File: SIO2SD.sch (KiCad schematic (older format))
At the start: 17 parts, among them J203 Micro_SD_Card, J204 ISP, J205 SIO, J206 SIOLED, U200 ATmega32-16AU, U201 74HC245, U202 LM2936-3.3, Y200 Crystal

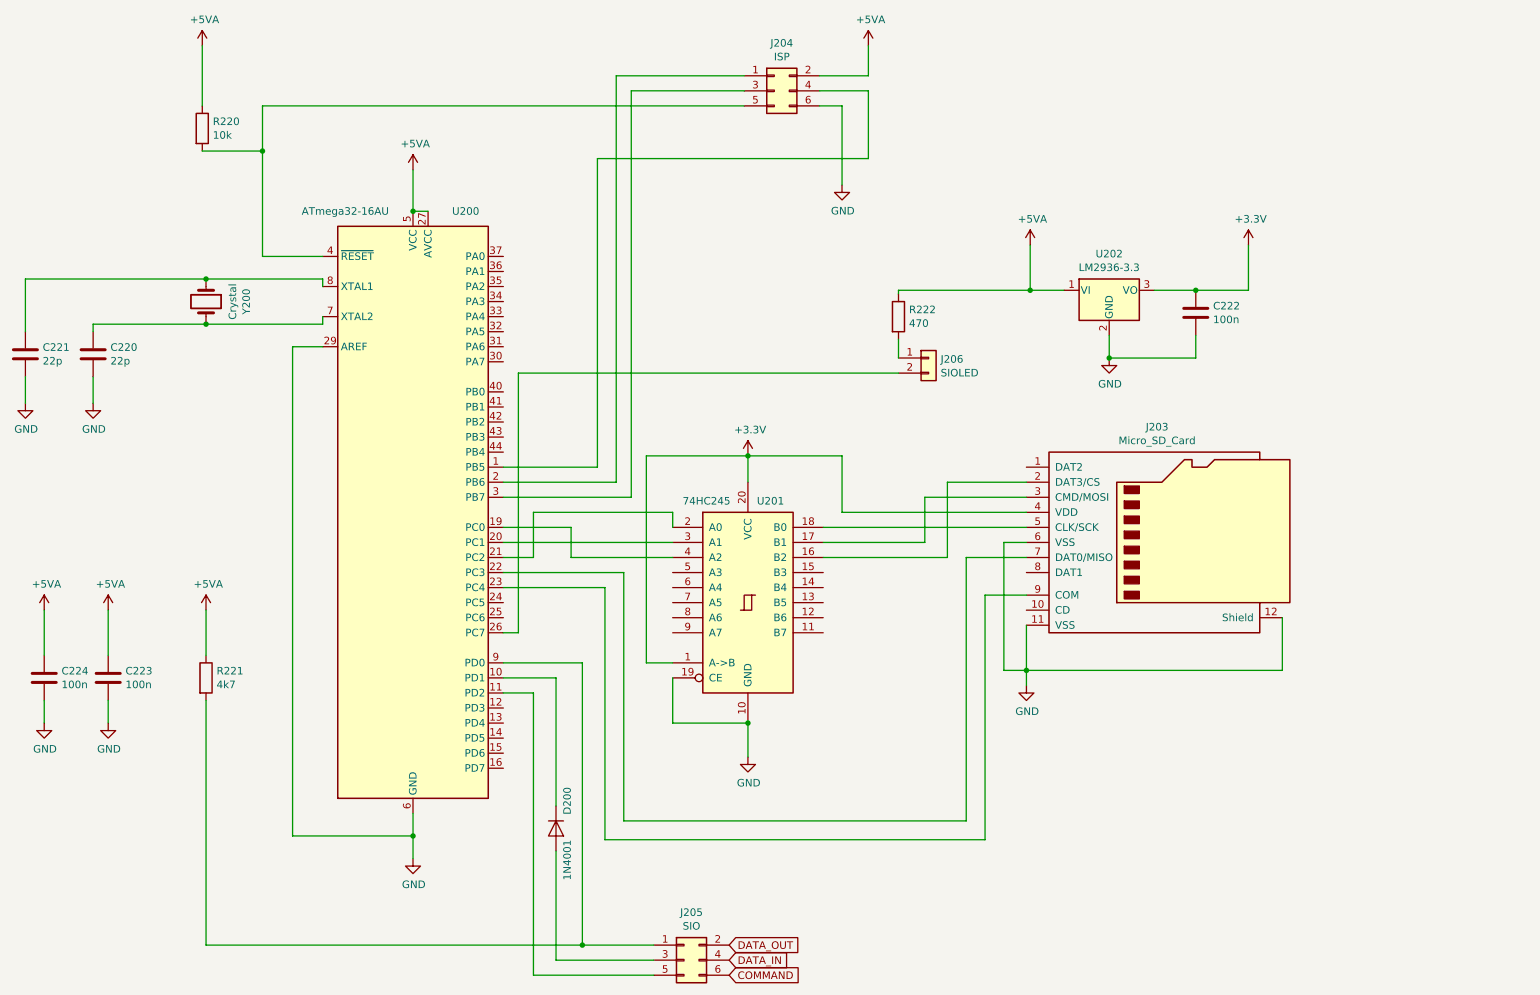
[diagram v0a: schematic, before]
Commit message: Final Atmega32
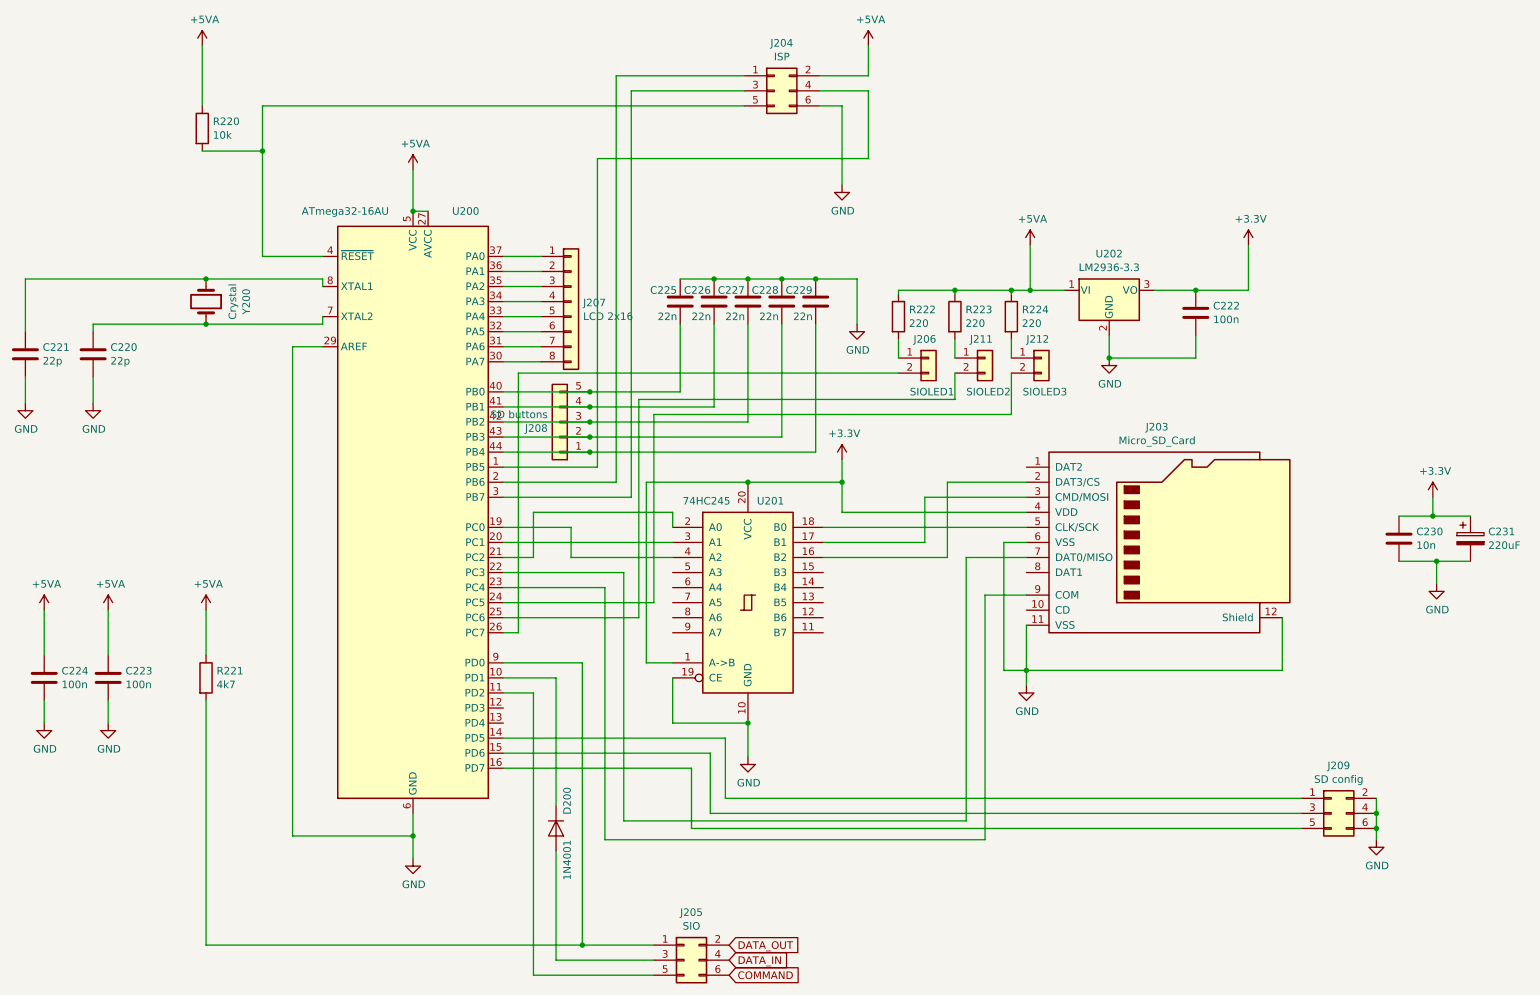
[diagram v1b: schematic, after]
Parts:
- added C225, C226, C227, C228, C229: 22n, Capacitor_SMD:C_1206_3216Metric_Pad1.42x1.75mm_HandSolder, symbol Device:C
- added C230: 10n, Capacitor_SMD:C_1206_3216Metric_Pad1.42x1.75mm_HandSolder, symbol Device:C
- added C231: 220uF, Capacitor_Tantalum_SMD:CP_EIA-7343-40_Kemet-Y_Pad2.25x2.55mm_HandSolder, symbol Device:CP
- added J207: LCD 2x16, Connector_PinHeader_2.54mm:PinHeader_1x08_P2.54mm_Vertical, symbol Connector_Generic:Conn_01x08
- added J208: SD buttons, Connector_PinHeader_2.54mm:PinHeader_1x05_P2.54mm_Vertical, symbol Connector_Generic:Conn_01x05
- added J209: SD config, Connector_PinHeader_2.54mm:PinHeader_2x03_P2.54mm_Vertical, symbol Connector_Generic:Conn_02x03_Odd_Even
- added J211: SIOLED2, Connector_PinHeader_2.54mm:PinHeader_1x02_P2.54mm_Vertical, symbol Connector_Generic:Conn_01x02
- added J212: SIOLED3, Connector_PinHeader_2.54mm:PinHeader_1x02_P2.54mm_Vertical, symbol Connector_Generic:Conn_01x02
- added R223, R224: 220, Resistor_SMD:R_1206_3216Metric_Pad1.42x1.75mm_HandSolder, symbol Device:R
- J206: value SIOLED -> SIOLED1
- R222: value 470 -> 220
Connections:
- net +3V3: now also C230.1, C231.1
- net +5VA: now also R223.1, R224.1
- net GND: now also C225.1, C226.1, C227.1, C228.1, C229.1, C230.2, C231.2, J209.2 (Pin_2), J209.4 (Pin_4), J209.6 (Pin_6)
- net at U200.14 (PD5): now also J209.1 (Pin_1)
- net at U200.15 (PD6): now also J209.3 (Pin_3)
- net at U200.16 (PD7): now also J209.5 (Pin_5)
- net at U200.24 (PC5): now also J212.2 (Pin_2)
- net at U200.25 (PC6): now also J211.2 (Pin_2)
- net at U200.30 (PA7): now also J207.8 (Pin_8)
- net at U200.31 (PA6): now also J207.7 (Pin_7)
- net at U200.32 (PA5): now also J207.6 (Pin_6)
- net at U200.33 (PA4): now also J207.5 (Pin_5)
- net at U200.34 (PA3): now also J207.4 (Pin_4)
- net at U200.35 (PA2): now also J207.3 (Pin_3)
- net at U200.36 (PA1): now also J207.2 (Pin_2)
- net at U200.37 (PA0): now also J207.1 (Pin_1)
- net at U200.40 (PB0): now also C225.2, J208.5 (Pin_5)
- net at U200.41 (PB1): now also C226.2, J208.4 (Pin_4)
- net at U200.42 (PB2): now also C227.2, J208.3 (Pin_3)
- net at U200.43 (PB3): now also C228.2, J208.2 (Pin_2)
- net at U200.44 (PB4): now also C229.2, J208.1 (Pin_1)
- new net: J211.1 (Pin_1), R223.2
- new net: J212.1 (Pin_1), R224.2

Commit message: final inspection
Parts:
- added J213: SD_conn, Connector_PinHeader_2.54mm:PinHeader_1x07_P2.54mm_Vertical, symbol Connector_Generic:Conn_01x07
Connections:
- net +3V3: now also J213.3 (Pin_3)
- net GND: now also J213.7 (Pin_7)
- net at J203.7 (DAT0/MISO), U200.22 (PC3): now also J213.1 (Pin_1)
- net at J203.9 (COM), U200.23 (PC4): now also J213.6 (Pin_6)
- net at J203.2 (DAT3/CS), U201.16 (B2): now also J213.5 (Pin_5)
- net at J203.3 (CMD/MOSI), U201.17 (B1): now also J213.4 (Pin_4)
- net at J203.5 (CLK/SCK), U201.18 (B0): now also J213.2 (Pin_2)
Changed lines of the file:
@@
 $EndComp
 Wire Wire Line
-	6350 4225 7700 4225
-Wire Wire Line
-	6350 4325 7025 4325
+	6350 4225 6975 4225
+Wire Wire Line
+	6350 4325 6825 4325
 Wire Wire Line
 	7025 4325 7025 4025
@@
 	7025 4025 7700 4025
 Wire Wire Line
-	6350 4425 7175 4425
-Wire Wire Line
 	7175 4425 7175 3925
 Wire Wire Line
@@
 	5025 6175 7300 6175
 Wire Wire Line
-	7300 6175 7300 4425
+	7300 6175 7300 5775
 Wire Wire Line
 	7300 4425 7700 4425
@@
 Wire Wire Line
 	4900 6300 7425 6300
-Wire Wire Line
-	7425 6300 7425 4675
 Wire Wire Line
 	7425 4675 7700 4675
@@
 	5350 5125 5175 5125
 Wire Wire Line
-	7700 4125 6475 4125
+	7700 4125 6900 4125
 Wire Wire Line
 	7700 4325 7550 4325
@@
 	10175 4450 10425 4450
 $Comp
-L power:GND #PWR?
+L power:GND #PWR0311
 U 1 1 6306756B
 P 10425 4600
-F 0 "#PWR?" H 10425 4350 50  0001 C CNN
+F 0 "#PWR0311" H 10425 4350 50  0001 C CNN
 F 1 "GND" H 10430 4427 50  0000 C CNN
 F 2 "" H 10425 4600 50  0001 C CNN
@@
 	10425 4450 10650 4450
 $Comp
-L power:+3.3V #PWR?
+L power:+3.3V #PWR0312
 U 1 1 6306F659
 P 10400 4025
-F 0 "#PWR?" H 10400 3875 50  0001 C CNN
+F 0 "#PWR0312" H 10400 3875 50  0001 C CNN
 F 1 "+3.3V" H 10415 4198 50  0000 C CNN
 F 2 "" H 10400 4025 50  0001 C CNN
@@
 Wire Wire Line
 	10400 4150 10650 4150
+$Comp
+L Connector_Generic:Conn_01x07 J213
+U 1 1 63031993
+P 6550 5475
+F 0 "J213" H 6468 4950 50  0000 C CNN
+F 1 "SD_conn" H 6468 5041 50  0000 C CNN
+F 2 "Connector_PinHeader_2.54mm:PinHeader_1x07_P2.54mm_Vertical" H 6550 5475 50  0001 C CNN
+F 3 "~" H 6550 5475 50  0001 C CNN
+	1    6550 5475
+	-1   0    0    1
+$EndComp
+Connection ~ 6825 4325
+Wire Wire Line
+	6825 4325 7025 4325
+Connection ~ 6900 4125
+Wire Wire Line
+	6900 4125 6475 4125
+Connection ~ 6975 4225
+Wire Wire Line
+	6975 4225 7700 4225
+Connection ~ 7550 4325
+Wire Wire Line
+	7425 4675 7425 5275
+Wire Wire Line
+	6750 5775 7300 5775
+Connection ~ 7300 5775
+Wire Wire Line
+	7300 5775 7300 4425
+Wire Wire Line
+	6975 5675 6750 5675
+Wire Wire Line
+	6975 4225 6975 5675
+Wire Wire Line
+	6750 5575 6900 5575
+Wire Wire Line
+	6900 4125 6900 5575
+Wire Wire Line
+	6825 5475 6750 5475
+Wire Wire Line
+	6825 4325 6825 5475
+Wire Wire Line
+	6350 4425 6450 4425
+Wire Wire Line
+	6450 4425 6450 5375
+Wire Wire Line
+	6450 5375 6750 5375
+Connection ~ 6450 4425
+Wire Wire Line
+	6450 4425 7175 4425
+Wire Wire Line
+	6750 5275 7425 5275
+Connection ~ 7425 5275
+Wire Wire Line
+	7425 5275 7425 6300
+Wire Wire Line
+	7125 4325 7125 5175
+Wire Wire Line
+	7125 5175 6750 5175
+Wire Wire Line
+	7125 4325 7550 4325
 $EndSCHEMATC

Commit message: Final inspection
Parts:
- Y200: value Crystal -> 14,31818 MHz
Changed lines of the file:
@@
 P 2250 2725
 F 0 "Y200" H 2250 2993 50  0000 C CNN
-F 1 "Crystal" H 2250 2902 50  0000 C CNN
+F 1 "14,31818 MHz" H 2250 2902 50  0000 C CNN
 F 2 "Crystal:Crystal_HC18-U_Vertical" H 2250 2725 50  0001 C CNN
 F 3 "~" H 2250 2725 50  0001 C CNN
